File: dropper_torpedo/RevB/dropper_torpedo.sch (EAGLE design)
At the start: 65 parts, among them CON1 SM03B-GHS-TB, CON2 SM03B-GHS-TB, CON3 MOLEX_5566-2, CON4 MOLEX_5566-2, CON6 MOLEX_5566-2, Q1 SI4896DY-T1-E3, Q2 SI4896DY-T1-E3, Q3 IRL6372TRPBF, Q4 IRL6372TRPBF, U1 LTV-355T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

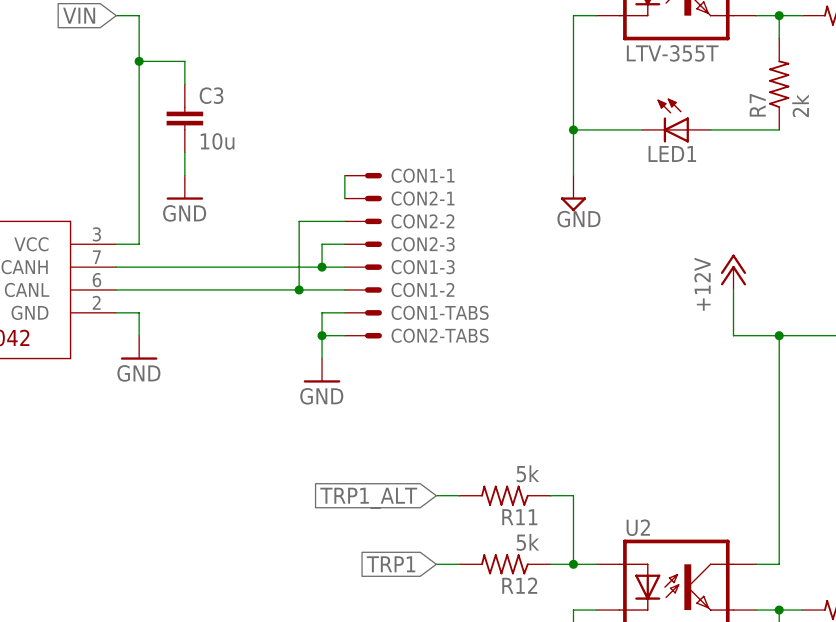
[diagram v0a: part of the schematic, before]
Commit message: dropper_torpedo: swapped out 3 pin JST for standards-based 4-pin
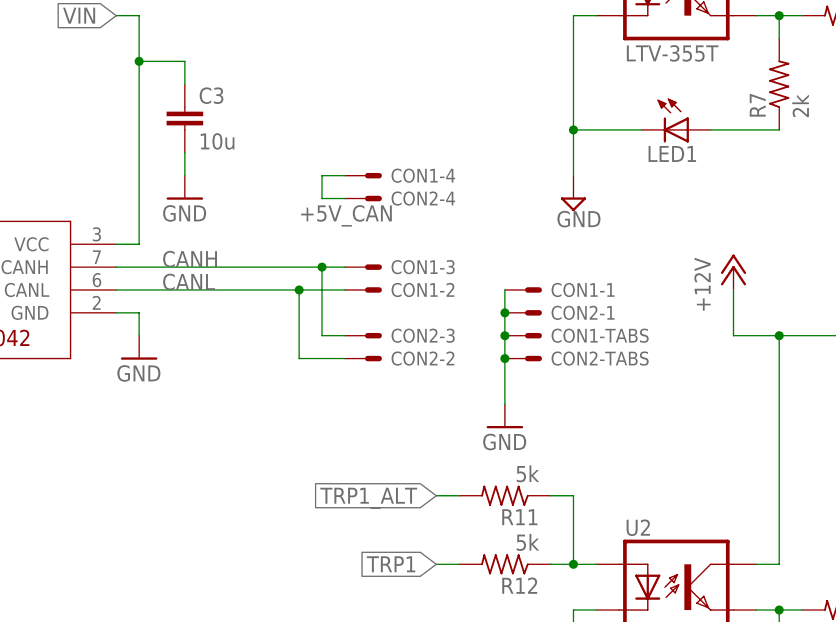
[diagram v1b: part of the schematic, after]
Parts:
- CON1, CON2: value SM03B-GHS-TB -> SM04B-GHS-TB; device ARVP:SM03B-GHS-TB -> ARVP:SM04B-GHS-TB
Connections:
- removed net CANSH: CON1-1.S, CON2-1.S
- new net +5V_CAN: CON1-4.S, CON2-4.S
- net GND: now also CON1-1.S, CON2-1.S
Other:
- moved on the sheet: CON1-1, CON1-TABS, CON2-1, CON2-2, CON2-3, CON2-TABS
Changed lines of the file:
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@@
 <?xml version="1.0" encoding="utf-8"?>
 <!DOCTYPE eagle SYSTEM "eagle.dtd">
-<eagle version="9.5.2">
+<eagle version="9.6.1">
 <drawing>
 <settings>
@@
 <part name="R13" library="rcl" library_urn="urn:adsk.eagle:library:334" deviceset="R-US_" device="R0805" package3d_urn="urn:adsk.eagle:package:23553/2" value="1k"/>
 <part name="GND16" library="supply1" library_urn="urn:adsk.eagle:library:371" deviceset="GND" device=""/>
-<part name="CON1" library="ARVP" deviceset="SM03B-GHS-TB" device=""/>
-<part name="GND13" library="supply1" library_urn="urn:adsk.eagle:library:371" deviceset="GND" device=""/>
-<part name="CON2" library="ARVP" deviceset="SM03B-GHS-TB" device=""/>
 <part name="+3V32" library="supply1" library_urn="urn:adsk.eagle:library:371" deviceset="+3V3" device=""/>
 <part name="R9" library="rcl" library_urn="urn:adsk.eagle:library:334" deviceset="R-US_" device="R0805" package3d_urn="urn:adsk.eagle:package:23553/2" value="5k"/>
@@
 <part name="SUPPLY16" library="supply2" library_urn="urn:adsk.eagle:library:372" deviceset="+7V" device=""/>
 <part name="SUPPLY17" library="supply2" library_urn="urn:adsk.eagle:library:372" deviceset="+7V" device=""/>
+<part name="CON1" library="ARVP" deviceset="SM04B-GHS-TB" device=""/>
+<part name="CON2" library="ARVP" deviceset="SM04B-GHS-TB" device=""/>
+<part name="GND13" library="supply1" library_urn="urn:adsk.eagle:library:371" deviceset="GND" device=""/>
 </parts>
 <sheets>
@@
 <attribute name="VALUE" x="154.94" y="38.1" size="1.778" layer="96"/>
 </instance>
-<instance part="CON1" gate="-1" x="215.9" y="83.82" smashed="yes">
-<attribute name="NAME" x="220.98" y="83.058" size="1.524" layer="95"/>
-</instance>
-<instance part="CON1" gate="-2" x="215.9" y="71.12" smashed="yes">
-<attribute name="NAME" x="220.98" y="70.358" size="1.524" layer="95"/>
-</instance>
-<instance part="CON1" gate="-3" x="215.9" y="73.66" smashed="yes">
-<attribute name="NAME" x="220.98" y="72.898" size="1.524" layer="95"/>
-</instance>
-<instance part="CON1" gate="-TABS" x="215.9" y="68.58" smashed="yes">
-<attribute name="NAME" x="220.98" y="67.818" size="1.524" layer="95"/>
-</instance>
-<instance part="GND13" gate="1" x="213.36" y="60.96" smashed="yes">
-<attribute name="VALUE" x="210.82" y="58.42" size="1.778" layer="96"/>
-</instance>
-<instance part="CON2" gate="-1" x="215.9" y="81.28" smashed="yes">
-<attribute name="NAME" x="220.98" y="80.518" size="1.524" layer="95"/>
-</instance>
-<instance part="CON2" gate="-2" x="215.9" y="78.74" smashed="yes">
-<attribute name="NAME" x="220.98" y="77.978" size="1.524" layer="95"/>
-</instance>
-<instance part="CON2" gate="-3" x="215.9" y="76.2" smashed="yes">
-<attribute name="NAME" x="220.98" y="75.438" size="1.524" layer="95"/>
-</instance>
-<instance part="CON2" gate="-TABS" x="215.9" y="66.04" smashed="yes">
-<attribute name="NAME" x="220.98" y="65.278" size="1.524" layer="95"/>
-</instance>
 <instance part="+3V32" gate="G$1" x="154.94" y="137.16" smashed="yes">
 <attribute name="VALUE" x="152.4" y="132.08" size="1.778" layer="96" rot="R90"/>
@@
 <instance part="CON6" gate="G$2" x="304.8" y="121.92" smashed="yes">
 <attribute name="NAME" x="309.88" y="121.158" size="1.524" layer="95"/>
+</instance>
+<instance part="CON1" gate="-1" x="233.68" y="71.12" smashed="yes">
+<attribute name="NAME" x="238.76" y="70.358" size="1.524" layer="95"/>
+</instance>
+<instance part="CON1" gate="-2" x="215.9" y="71.12" smashed="yes">
+<attribute name="NAME" x="220.98" y="70.358" size="1.524" layer="95"/>
+</instance>
+<instance part="CON1" gate="-3" x="215.9" y="73.66" smashed="yes">
+<attribute name="NAME" x="220.98" y="72.898" size="1.524" layer="95"/>
+</instance>
+<instance part="CON1" gate="-TABS" x="233.68" y="66.04" smashed="yes">
+<attribute name="NAME" x="238.76" y="65.278" size="1.524" layer="95"/>
+</instance>
+<instance part="CON1" gate="-4" x="215.9" y="83.82" smashed="yes">
+<attribute name="NAME" x="220.98" y="83.058" size="1.524" layer="95"/>
+</instance>
+<instance part="CON2" gate="-1" x="233.68" y="68.58" smashed="yes">
+<attribute name="NAME" x="238.76" y="67.818" size="1.524" layer="95"/>
+</instance>
+<instance part="CON2" gate="-2" x="215.9" y="63.5" smashed="yes">
+<attribute name="NAME" x="220.98" y="62.738" size="1.524" layer="95"/>
+</instance>
+<instance part="CON2" gate="-3" x="215.9" y="66.04" smashed="yes">
+<attribute name="NAME" x="220.98" y="65.278" size="1.524" layer="95"/>
+</instance>
+<instance part="CON2" gate="-TABS" x="233.68" y="63.5" smashed="yes">
+<attribute name="NAME" x="238.76" y="62.738" size="1.524" layer="95"/>
+</instance>
+<instance part="CON2" gate="-4" x="215.9" y="81.28" smashed="yes">
+<attribute name="NAME" x="220.98" y="80.518" size="1.524" layer="95"/>
+</instance>
+<instance part="GND13" gate="1" x="233.68" y="55.88" smashed="yes">
+<attribute name="VALUE" x="231.14" y="53.34" size="1.778" layer="96"/>
 </instance>
 </instances>
@@
 </segment>
 <segment>
+<pinref part="CON2" gate="-TABS" pin="S"/>
+<wire x1="233.68" y1="63.5" x2="233.68" y2="58.42" width="0.1524" layer="91"/>
 <pinref part="GND13" gate="1" pin="GND"/>
-<wire x1="213.36" y1="63.5" x2="213.36" y2="66.04" width="0.1524" layer="91"/>
+<pinref part="CON1" gate="-1" pin="S"/>
+<pinref part="CON2" gate="-1" pin="S"/>
+<wire x1="233.68" y1="71.12" x2="233.68" y2="68.58" width="0.1524" layer="91"/>
 <pinref part="CON1" gate="-TABS" pin="S"/>
-<wire x1="213.36" y1="66.04" x2="213.36" y2="68.58" width="0.1524" layer="91"/>
-<wire x1="213.36" y1="68.58" x2="215.9" y2="68.58" width="0.1524" layer="91"/>
-<pinref part="CON2" gate="-TABS" pin="S"/>
-<wire x1="213.36" y1="66.04" x2="215.9" y2="66.04" width="0.1524" layer="91"/>
-<junction x="213.36" y="66.04"/>
+<wire x1="233.68" y1="68.58" x2="233.68" y2="66.04" width="0.1524" layer="91"/>
+<junction x="233.68" y="68.58"/>
+<wire x1="233.68" y1="66.04" x2="233.68" y2="63.5" width="0.1524" layer="91"/>
+<junction x="233.68" y="66.04"/>
+<junction x="233.68" y="63.5"/>
 </segment>
 </net>
@@
 <segment>
 <pinref part="U3" gate="G$1" pin="CANH"/>
+<wire x1="190.5" y1="73.66" x2="213.36" y2="73.66" width="0.1524" layer="91"/>
+<label x="195.58" y="73.66" size="1.778" layer="95"/>
+<wire x1="213.36" y1="73.66" x2="213.36" y2="66.04" width="0.1524" layer="91"/>
+<pinref part="CON2" gate="-3" pin="S"/>
+<wire x1="213.36" y1="66.04" x2="215.9" y2="66.04" width="0.1524" layer="91"/>
 <pinref part="CON1" gate="-3" pin="S"/>
-<wire x1="190.5" y1="73.66" x2="213.36" y2="73.66" width="0.1524" layer="91"/>
-<pinref part="CON2" gate="-3" pin="S"/>
 <wire x1="213.36" y1="73.66" x2="215.9" y2="73.66" width="0.1524" layer="91"/>
-<wire x1="215.9" y1="76.2" x2="213.36" y2="76.2" width="0.1524" layer="91"/>
-<wire x1="213.36" y1="76.2" x2="213.36" y2="73.66" width="0.1524" layer="91"/>
 <junction x="213.36" y="73.66"/>
 </segment>
@@
 <segment>
 <pinref part="U3" gate="G$1" pin="CANL"/>
+<wire x1="190.5" y1="71.12" x2="210.82" y2="71.12" width="0.1524" layer="91"/>
+<label x="195.58" y="71.12" size="1.778" layer="95"/>
+<wire x1="210.82" y1="71.12" x2="210.82" y2="63.5" width="0.1524" layer="91"/>
+<pinref part="CON2" gate="-2" pin="S"/>
+<wire x1="210.82" y1="63.5" x2="215.9" y2="63.5" width="0.1524" layer="91"/>
 <pinref part="CON1" gate="-2" pin="S"/>
-<wire x1="190.5" y1="71.12" x2="210.82" y2="71.12" width="0.1524" layer="91"/>
-<pinref part="CON2" gate="-2" pin="S"/>
 <wire x1="210.82" y1="71.12" x2="215.9" y2="71.12" width="0.1524" layer="91"/>
-<wire x1="215.9" y1="78.74" x2="210.82" y2="78.74" width="0.1524" layer="91"/>
-<wire x1="210.82" y1="78.74" x2="210.82" y2="71.12" width="0.1524" layer="91"/>
 <junction x="210.82" y="71.12"/>
-</segment>
-</net>
-<net name="CANSH" class="0">
-<segment>
-<pinref part="CON1" gate="-1" pin="S"/>
-<pinref part="CON2" gate="-1" pin="S"/>
-<wire x1="215.9" y1="83.82" x2="215.9" y2="81.28" width="0.1524" layer="91"/>
 </segment>
 </net>
@@
 </segment>
 </net>
+<net name="+5V_CAN" class="0">
+<segment>
+<wire x1="213.36" y1="83.82" x2="213.36" y2="81.28" width="0.1524" layer="91"/>
+<label x="210.82" y="78.74" size="1.778" layer="95"/>
+<pinref part="CON1" gate="-4" pin="S"/>
+<wire x1="215.9" y1="83.82" x2="213.36" y2="83.82" width="0.1524" layer="91"/>
+<pinref part="CON2" gate="-4" pin="S"/>
+<wire x1="215.9" y1="81.28" x2="213.36" y2="81.28" width="0.1524" layer="91"/>
+</segment>
+</net>
